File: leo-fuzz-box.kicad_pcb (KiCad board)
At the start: 2 copper layers, 22.5 x 39.8 mm, 24 parts, among them J1 IN, J2 Conn_01x04_Female, J3 OUT, J4 Power, Q1 2N3565, Q2 2N3565, SW1 Fuzz/Normal

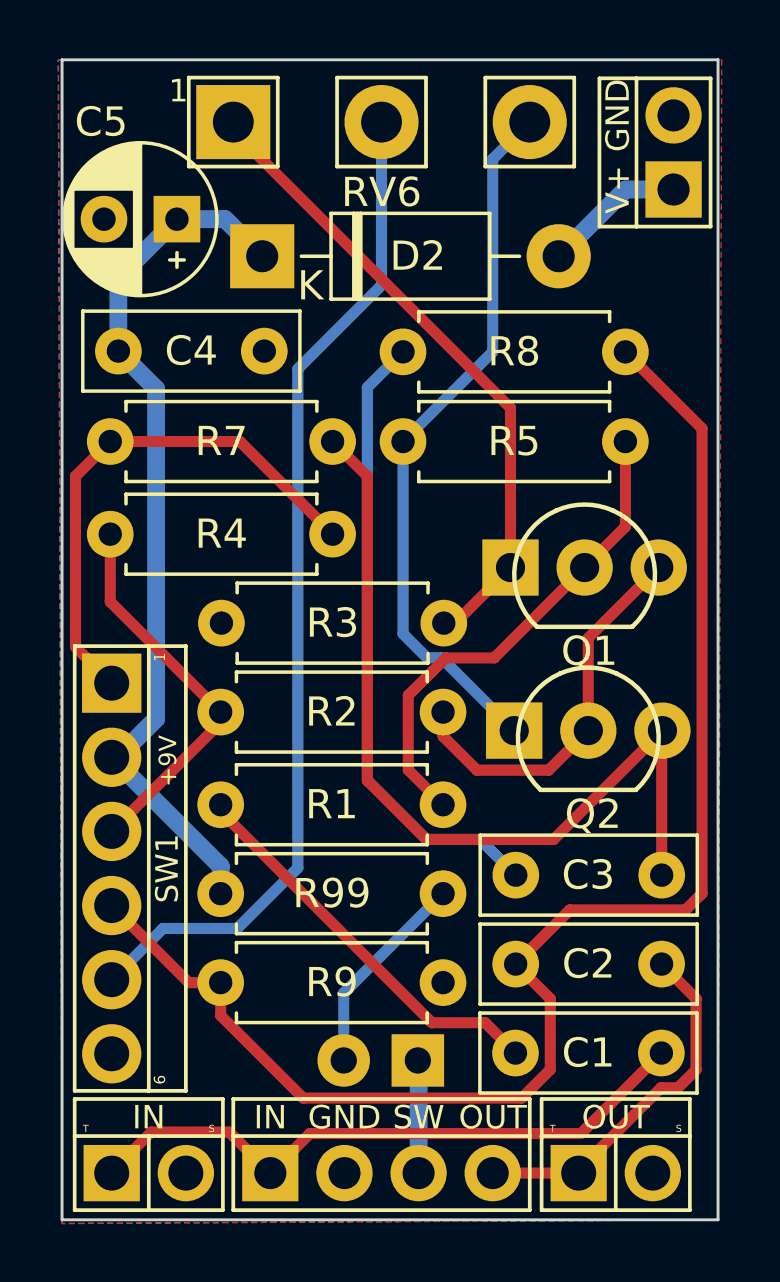
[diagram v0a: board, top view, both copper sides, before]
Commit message: v0.2: tighter layout, Gerbers sent to Oshpark
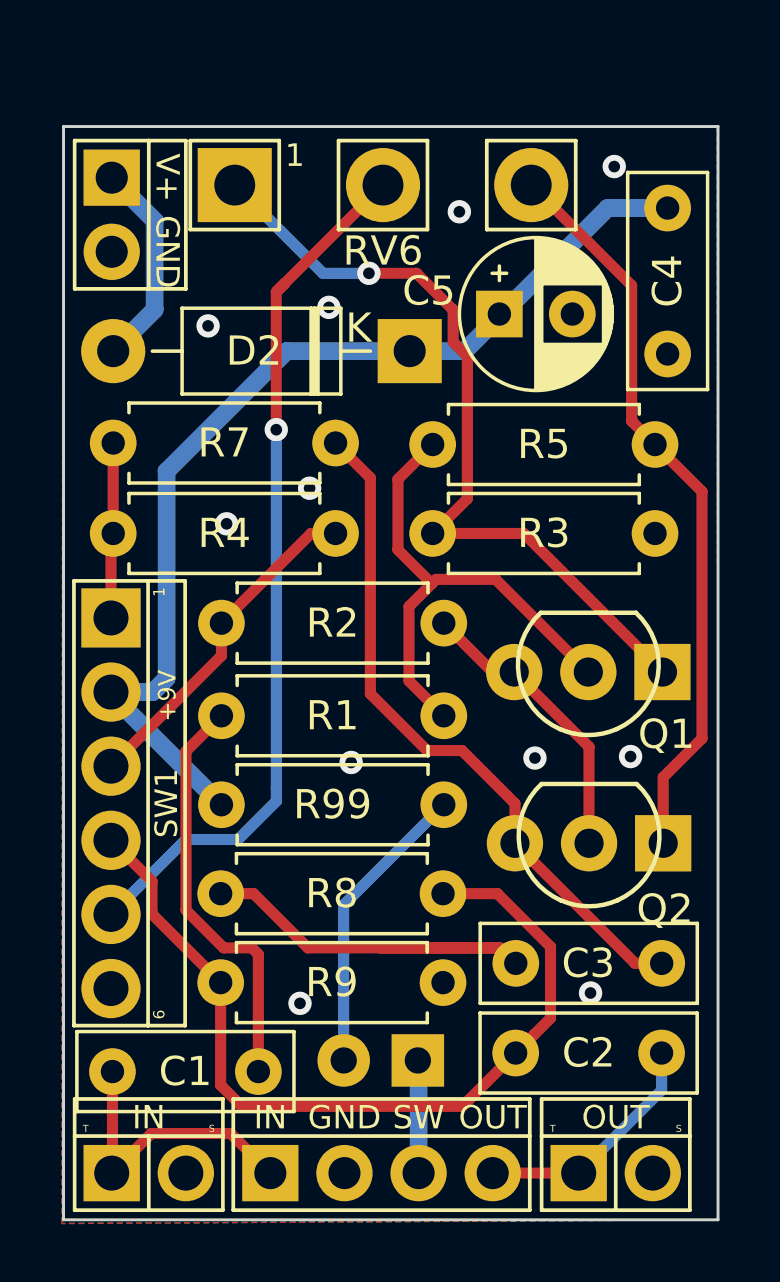
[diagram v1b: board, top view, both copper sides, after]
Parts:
- moved J4 20.6 mm to (90.2, 45.2), turned to -90 degrees
- moved R8 19.6 mm to (94.0, 65.9)
- moved C4 19.4 mm to (109.3, 42.4), turned to -90 degrees
- moved C1 18.8 mm to (90.2, 72.0), turned to 0 degrees
- moved C5 11.5 mm to (103.5, 46.1), turned to 0 degrees
- moved R4 7.72 mm to (97.9, 53.6), turned to 180 degrees
- moved R5 6.60 mm to (101.2, 50.5), turned to 0 degrees
- moved D2 6.01 mm to (100.4, 47.3), turned to 180 degrees
- moved Q2 3.86 mm to (106.6, 64.2), turned to 180 degrees
- moved Q1 3.58 mm to (106.6, 58.3), turned to 180 degrees
- moved R3 3.10 mm to (101.2, 53.6), turned to 0 degrees
- moved R1 3.05 mm to (94.0, 59.8)
- moved R2 3.05 mm to (94.0, 56.6)
- moved R99 3.05 mm to (101.6, 62.9)
- moved C2 3.05 mm to (104.1, 71.4)
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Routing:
- net Net-(C2-Pad1): track 50.0 -> 29.7 mm
- net Net-(R4-Pad2): track 18.2 -> 6.03 mm
- net IN: track 21.7 -> 10.0 mm
- net Net-(C3-Pad1): track 29.6 -> 23.7 mm
- net Net-(Q1-Pad1): track 22.3 -> 28.1 mm, vias 0 -> 1
- net Net-(C3-Pad2): track 21.6 -> 16.0 mm
- net +9V: track 30.2 -> 35.5 mm
- net OUT: track 12.6 -> 8.24 mm
- net Net-(RV6-Pad2): track 34.7 -> 30.6 mm, vias 0 -> 1
- net Net-(Q1-Pad3): track 13.4 -> 10.0 mm
- net Net-(D1-Pad2): track 7.12 -> 10.2 mm
- net Net-(D2-Pad2): track 4.25 -> 7.14 mm
- net Net-(R2-Pad1): track 13.3 -> 11.7 mm
- net Net-(Q2-Pad1): track 24.5 -> 25.5 mm
- net Net-(Q1-Pad2): track 17.0 -> 17.8 mm
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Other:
- board size 22.5 x 39.8 mm -> 22.4 x 37.5 mm

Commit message: v0.3: C2 goes between pot and switch
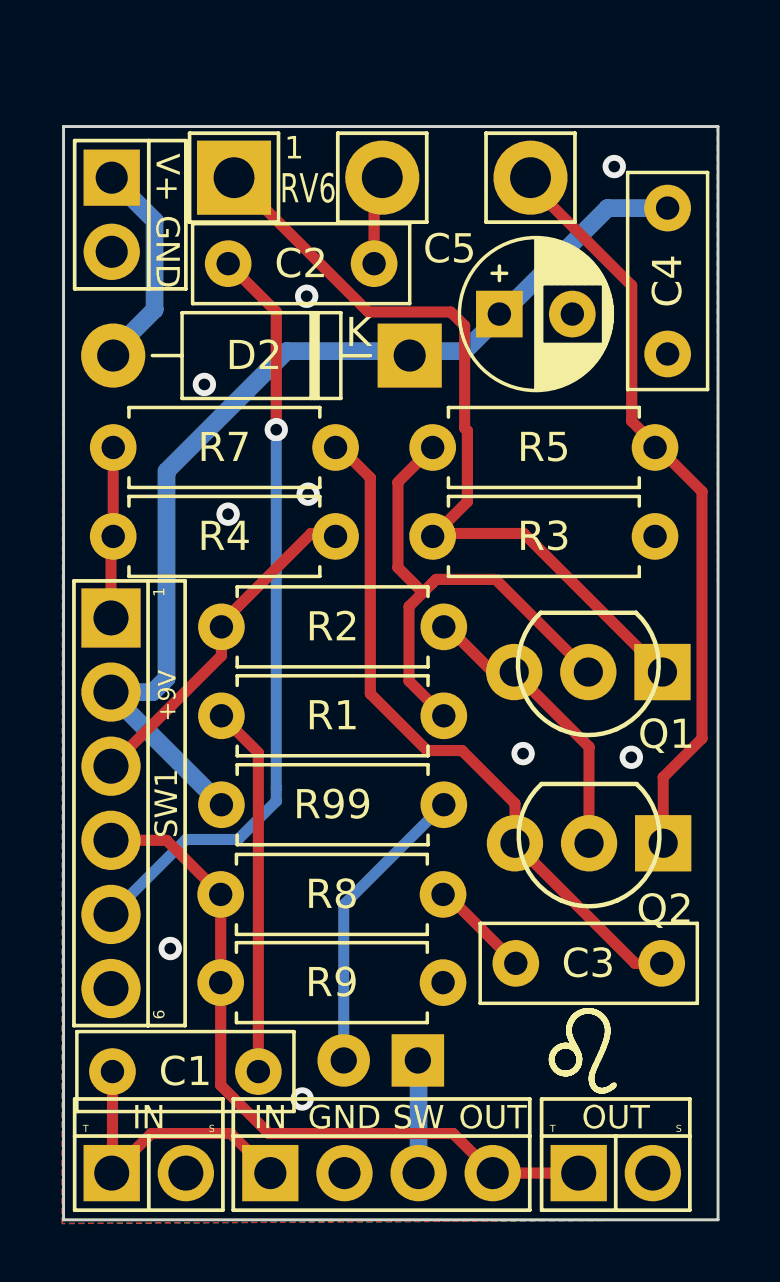
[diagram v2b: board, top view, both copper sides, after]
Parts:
- moved C2 27.5 mm to (99.2, 44.3), turned to 180 degrees
- moved R8 7.62 mm to (101.6, 65.9), turned to 180 degrees
- moved RV6 0.26 mm to (99.5, 41.4)
- moved D2 0.15 mm to (100.4, 47.5)
- moved R7 0.15 mm to (90.3, 50.6)
- moved R2 0.13 mm to (94.0, 56.8)
- moved R3 0.10 mm to (101.2, 53.7)
- moved R4 0.10 mm to (97.9, 53.7)
- moved R5 0.10 mm to (101.2, 50.6)
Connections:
- C2 pad 2: OUT -> Net-(C2-Pad2)
- R8 pad 2: Net-(C2-Pad1) -> OUT
- R9 pad 1: Net-(C2-Pad1) -> OUT
- RV6 pad 2: Net-(RV6-Pad2) -> Net-(C2-Pad1)
- SW1 pad 4: Net-(C2-Pad1) -> OUT
- SW1 pad 5: Net-(RV6-Pad2) -> Net-(C2-Pad2)
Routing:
- net Net-(RV6-Pad2): track 30.6 -> 0.00 mm, vias 1 -> 0
- net Net-(C2-Pad2): track 0.00 -> 26.4 mm, vias 0 -> 1
- net Net-(C2-Pad1): track 29.7 -> 3.39 mm
- net OUT: track 8.24 -> 24.6 mm
- net Net-(C3-Pad2): track 16.0 -> 3.47 mm
- net Net-(C1-Pad2): track 14.3 -> 12.7 mm
- net Net-(Q1-Pad1): track 28.1 -> 28.2 mm, vias 1 -> 0
- net GND: vias 11 -> 9
